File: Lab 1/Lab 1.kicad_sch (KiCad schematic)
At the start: 50 parts, among them K1 Fujitsu_FTR-LYCA005x, K10 Fujitsu_FTR-LYCA005x, K11 Fujitsu_FTR-LYCA005x, K12 Fujitsu_FTR-LYCA005x, K13 Fujitsu_FTR-LYCA005x, K14 Fujitsu_FTR-LYCA005x, K15 Fujitsu_FTR-LYCA005x, K2 Fujitsu_FTR-LYCA005x, K3 Fujitsu_FTR-LYCA005x, K4 Fujitsu_FTR-LYCA005x, K5 Fujitsu_FTR-LYCA005x, K6 Fujitsu_FTR-LYCA005x, K7 Fujitsu_FTR-LYCA005x, K8 Fujitsu_FTR-LYCA005x, K9 Fujitsu_FTR-LYCA005x, M1 Motor_DC, M2 Motor_DC, M3 Motor_DC, SW1 SW_Push, SW10 SW_Nidec_CAS-120A1, SW11 SW_Nidec_CAS-120A1, SW12 SW_Nidec_CAS-120A1, SW13 SW_Push, SW2 SW_Push_Open, SW3 SW_Push, SW4 SW_Push_Open, SW5 SW_Push, SW6 SW_Push, SW7 SW_Push, SW8 SW_Push, SW9 SW_Nidec_CAS-120A1

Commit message: Add fuses to A2-4
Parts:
- added F1, F2, F3: Fuse, symbol Device:Fuse
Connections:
- net at R4.2: now also F3.1; no longer D3.2 (A)
- net at R3.2: now also F2.1; no longer D2.2 (A)
- net at R2.2: now also F1.1; no longer D1.2 (A)
- new net: D2.2 (A), F2.2
- new net: D3.2 (A), F3.2
- new net: D1.2 (A), F1.2
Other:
- moved on the sheet: R2, R3

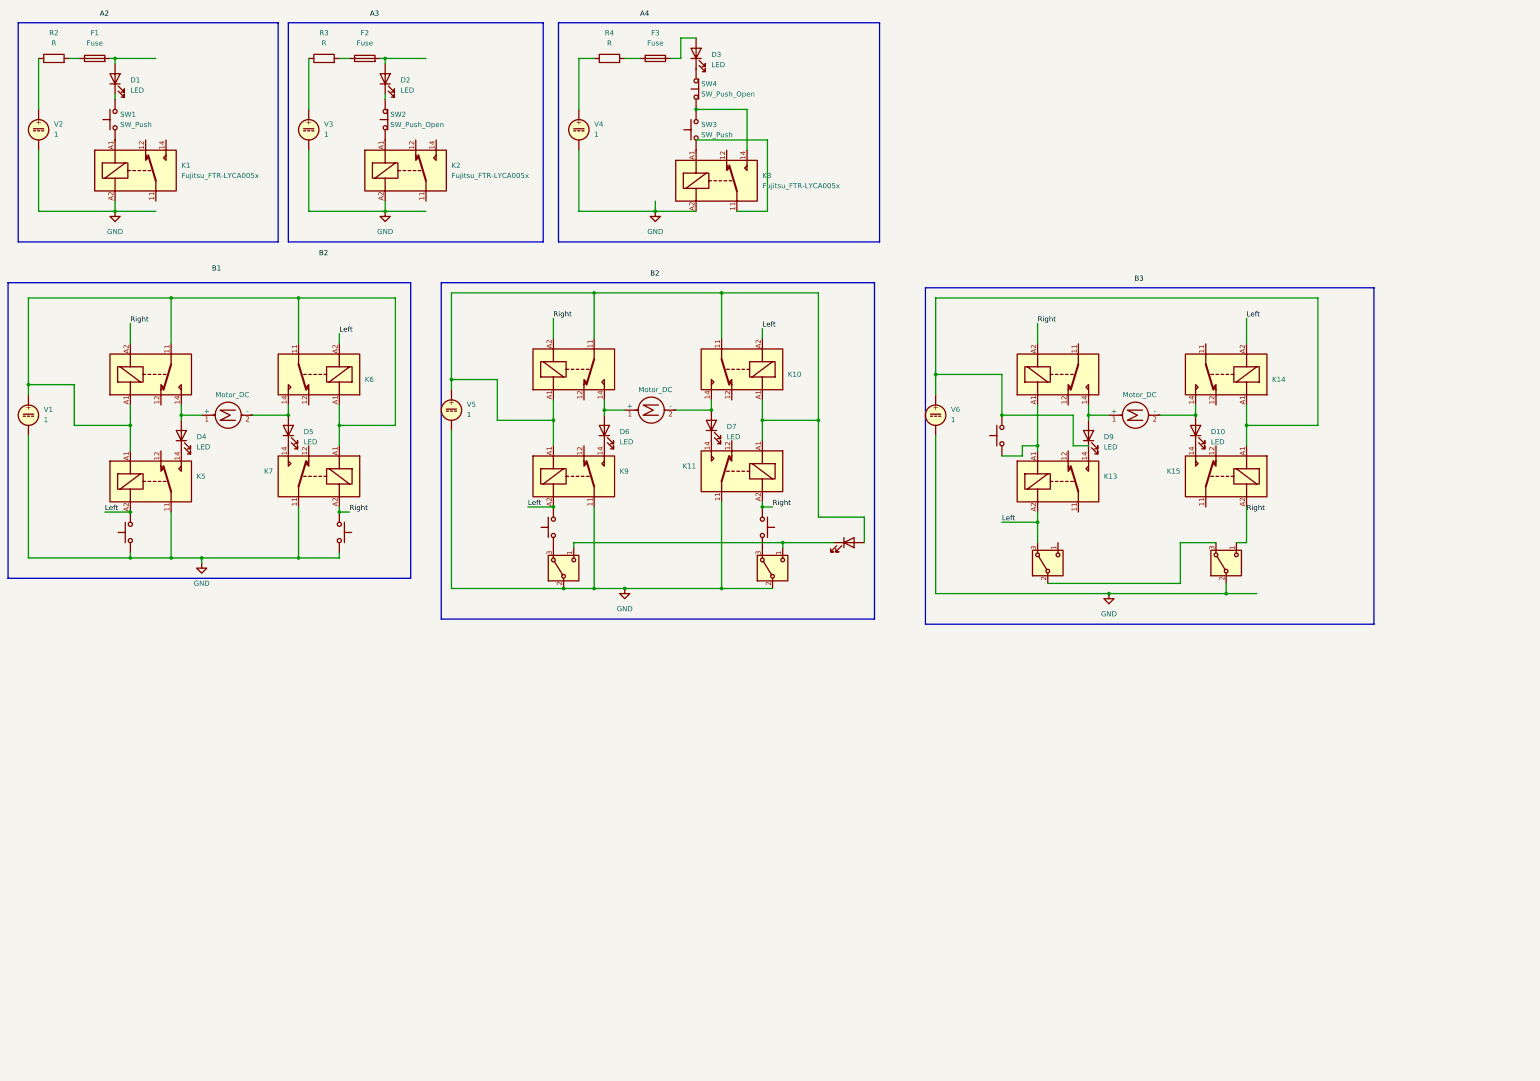
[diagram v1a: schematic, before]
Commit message: Redo B1 and B2 to use 2 relays
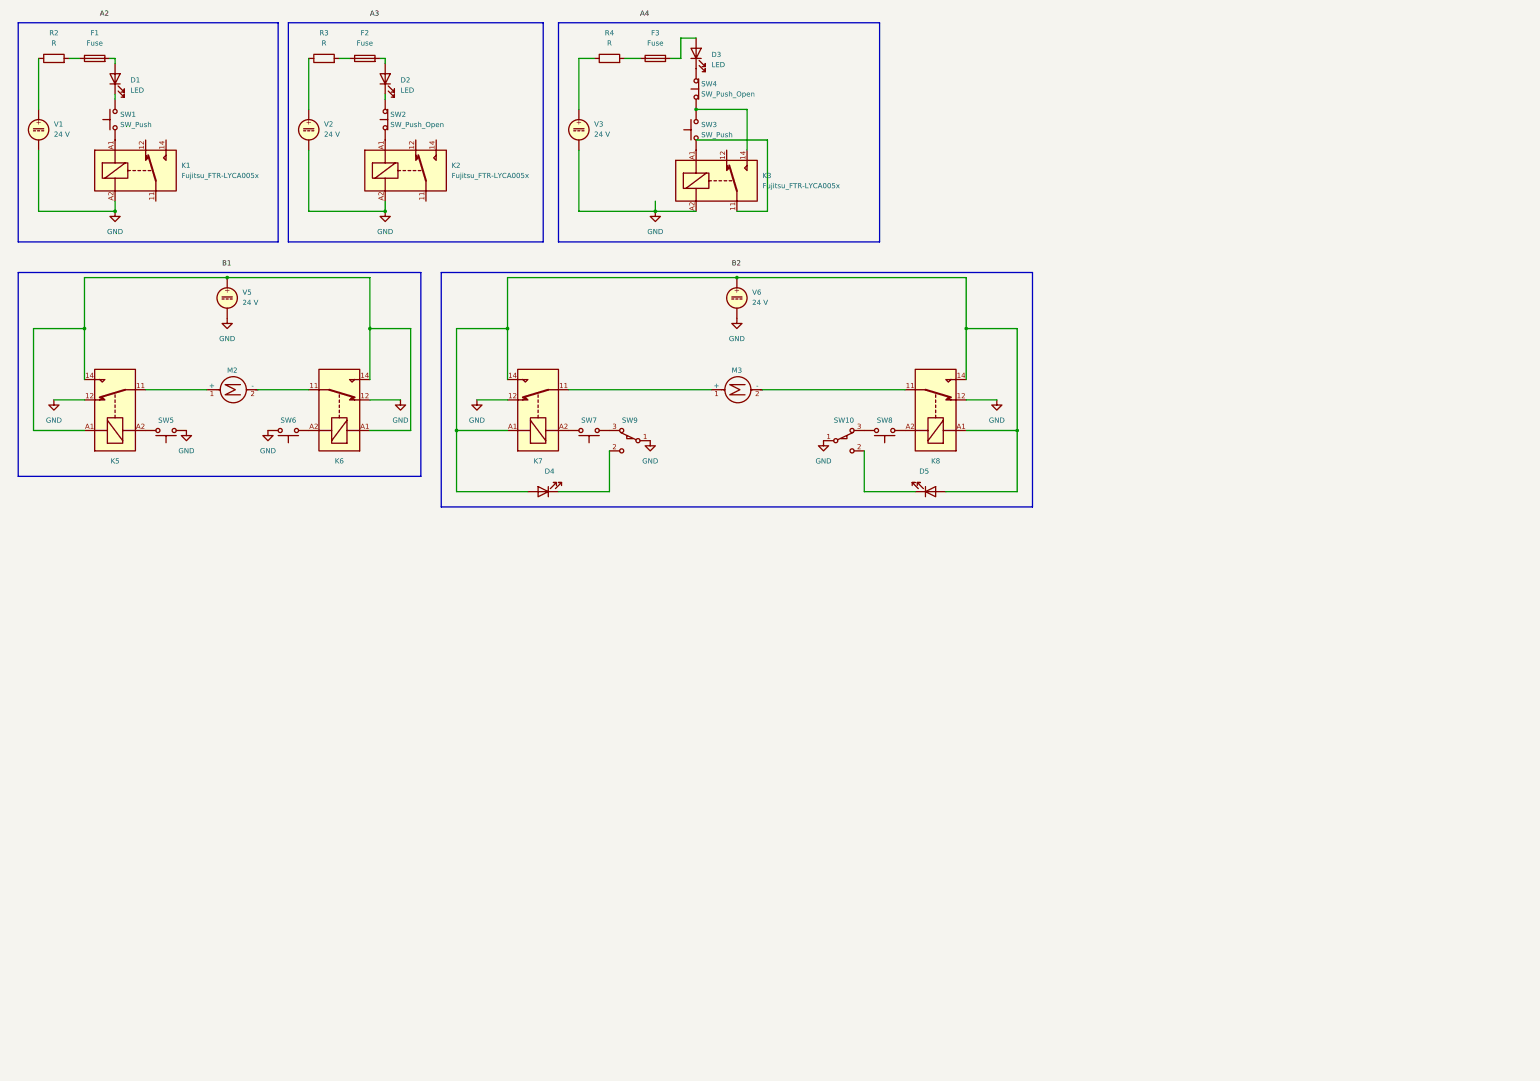
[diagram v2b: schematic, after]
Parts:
- removed D10, D6, D7, D8, D9: LED, symbol Device:LED
- removed K10, K11, K12, K13, K14, K15, K4, K9: Fujitsu_FTR-LYCA005x, Relay_THT:Relay_SPDT_Fujitsu_FTR-LYCA005x_FormC_Vertical, symbol Relay:Fujitsu_FTR-LYCA005x
- removed M1: Motor_DC, symbol Motor:Motor_DC
- removed SW10, SW11, SW12, SW9: SW_Nidec_CAS-120A1, Button_Switch_SMD:Nidec_Copal_CAS-120A, symbol Switch:SW_Nidec_CAS-120A1
- removed SW13: SW_Push, symbol Switch:SW_Push
- removed V1, V4: 1, symbol Simulation_SPICE:VDC
- added SW10, SW9: SW_SPDT_XKB_DMx-xxxx-1, symbol Switch:SW_SPDT_XKB_DMx-xxxx-1
- added V3: 24 V, symbol Simulation_SPICE:VDC
- V1: renamed from V2; value 1 -> 24 V
- V2: renamed from V3; value 1 -> 24 V
- V5, V6: value 1 -> 24 V
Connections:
- net GND: now also K5.12, K6.12, K7.12, K8.12, SW10.1 (A), SW9.1 (A), V3.2; no longer K5.11, K7.11
- net at R4.1: now also V3.1
- net at SW7.1: now also SW9.3 (C)
- net at K5.14: now also K5.A1, K6.14, K6.A1, V5.1; no longer D4.1 (K)
- net at D4.2 (A): now also D5.2 (A), K7.14, K7.A1, K8.14, K8.A1, V6.1
- net at M3.1 (+): now also K7.11
- net at M3.2 (-): now also K8.11
- net at M2.1 (+): now also K5.11; no longer K8.14
- net at SW8.1: now also SW10.3 (C)
- net at M2.2 (-): now also K6.11
- net at D5.1 (K): now also SW10.2 (B); no longer K7.14
- net Left: no longer names the net of K5.A2, SW5.2
- net Left: no longer K6.A2, SW7.2
- net Right: no longer names the net of K8.A2, SW8.2
- net Right: no longer K7.A2, SW6.2
- new net: K7.A2, SW7.2
- new net: K6.A2, SW6.2
- new net: D4.1 (K), SW9.2 (B)

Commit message: Add missing leds
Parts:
- added D4, D5, D6, D7: LED, symbol Device:LED
- renumbered D4 to D8, D5 to D9
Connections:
- net GND: now also D4.1 (K), D5.1 (K), D6.1 (K), D7.1 (K); no longer K5.12, K6.12, K7.12, K8.12
- new net: D5.2 (A), K5.12
- new net: D7.2 (A), K8.12
- new net: D6.2 (A), K7.12
- new net: D4.2 (A), K6.12

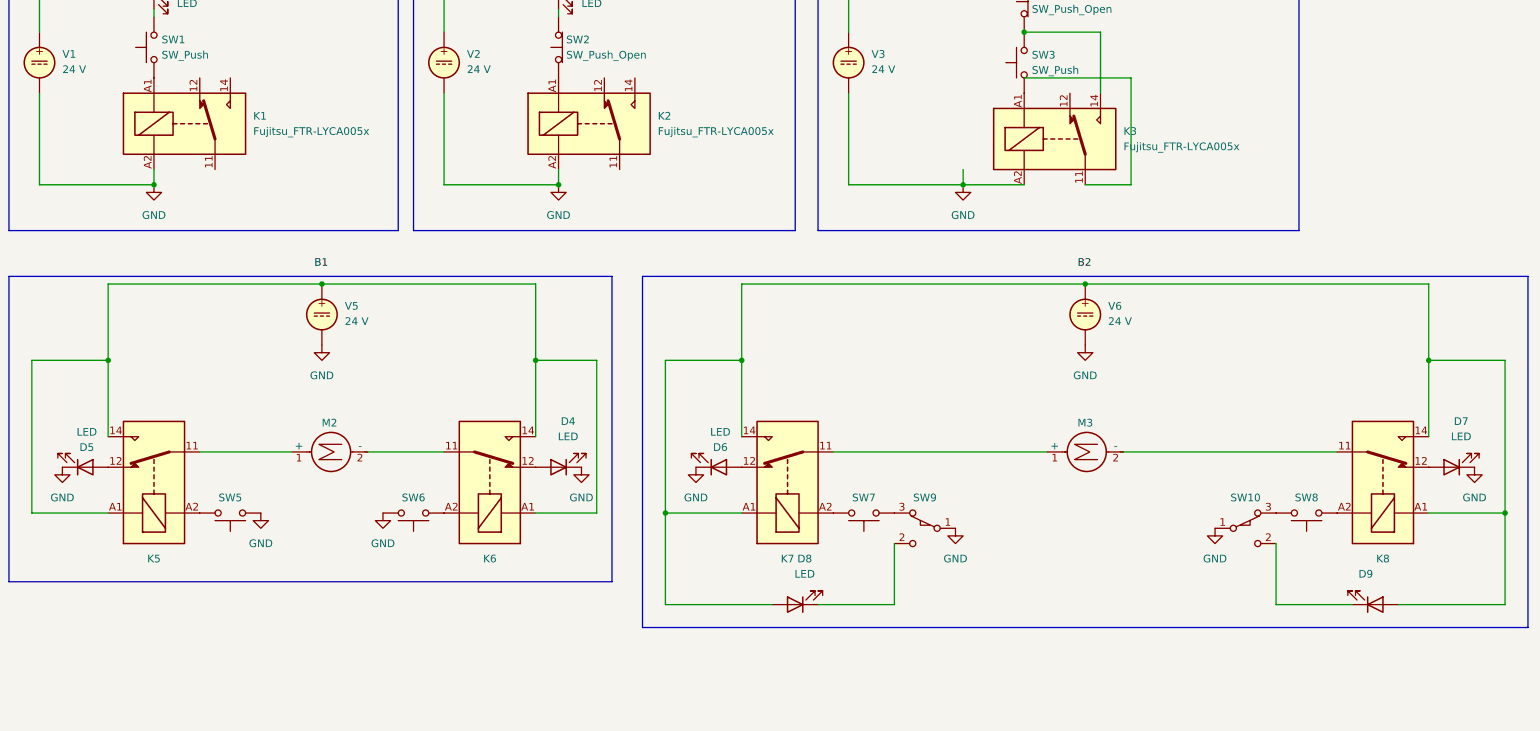
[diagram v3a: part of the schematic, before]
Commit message: Add START and STOP buttons to B2
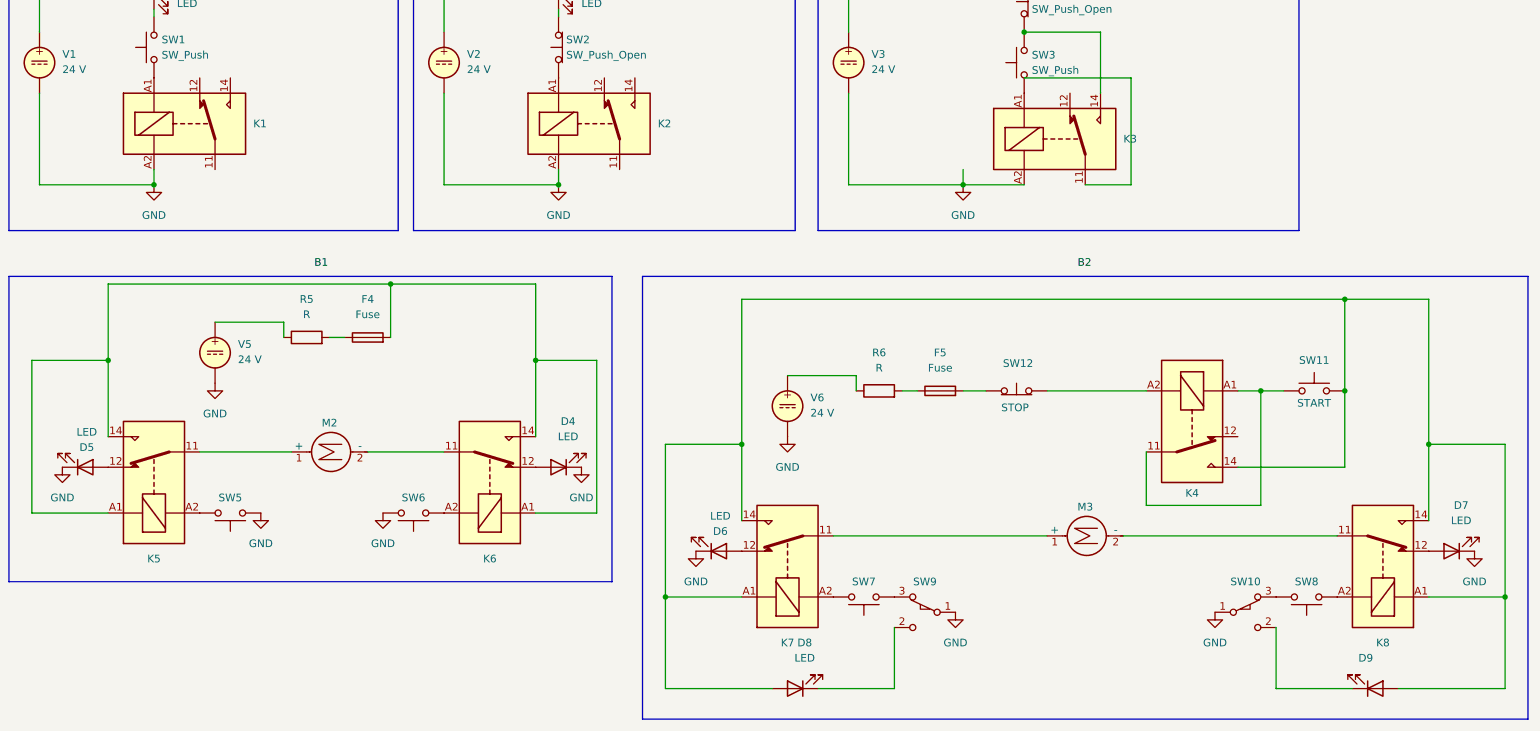
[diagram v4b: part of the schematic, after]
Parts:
- added F4, F5: Fuse, symbol Device:Fuse
- added K4: Fujitsu_FTR-LYCA005x, Relay_THT:Relay_SPDT_Fujitsu_FTR-LYCA005x_FormC_Vertical, symbol Relay:Fujitsu_FTR-LYCA005x
- added R5, R6: R, symbol Device:R
- added SW11: START, symbol Switch:SW_Push
- added SW12: STOP, symbol Switch:SW_Push_Open
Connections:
- net at K5.14, K5.A1, K6.14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: now also F4.2; no longer V5.1
- net at D8.2 (A), D9.2 (A), K7.14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: now also K4.14, SW11.2; no longer V6.1
- new net: K4.11, K4.A1, SW11.1
- new net: K4.A2, SW12.2 (B)
- new net: F4.1, R5.2
- new net: R5.1, V5.1
- new net: F5.2, SW12.1 (A)
- new net: R6.1, V6.1
- new net: F5.1, R6.2
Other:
- moved on the sheet: D6, D7, D8, D9, K7, K8, M3, SW10, SW7, SW8, SW9, V5

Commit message: Add B3
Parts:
- added D10, D11, D12, D13: LED, symbol Device:LED
- added F6: Fuse, symbol Device:Fuse
- added K10, K11, K12, K9: Fujitsu_FTR-LYCA005x, Relay_THT:Relay_SPDT_Fujitsu_FTR-LYCA005x_FormC_Vertical, symbol Relay:Fujitsu_FTR-LYCA005x
- added M4: Motor_DC, symbol Motor:Motor_DC
- added R7: R, symbol Device:R
- added SW13, SW14: SW_SPDT_XKB_DMx-xxxx-1, symbol Switch:SW_SPDT_XKB_DMx-xxxx-1
- added SW15: STOP, symbol Switch:SW_Push_Open
- added SW18: START, symbol Switch:SW_Push
- added V7: 24 V, symbol Simulation_SPICE:VDC
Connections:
- net GND: now also D10.1 (K), D11.1 (K), D12.1 (K), D13.1 (K), K12.11, V7.2
- new net: K11.A2, K12.14, K12.A1, SW14.1 (A)
- new net: D12.2 (A), SW14.2 (B)
- new net: K10.14, K11.14, K11.A1, K9.14, K9.A1, SW13.1 (A), SW18.2
- new net: D11.2 (A), SW13.2 (B)
- new net: K12.A2, SW13.3 (C)
- new net: R7.1, V7.1
- new net: F6.1, R7.2
- new net: K10.11, K10.A1, SW18.1
- new net: K10.A2, SW15.2 (B)
- new net: K12.12, K9.A2
- new net: K9.11, M4.1 (+)
- new net: D10.2 (A), K9.12
- new net: F6.2, SW15.1 (A)
- new net: K11.11, M4.2 (-)
- new net: D13.2 (A), K11.12

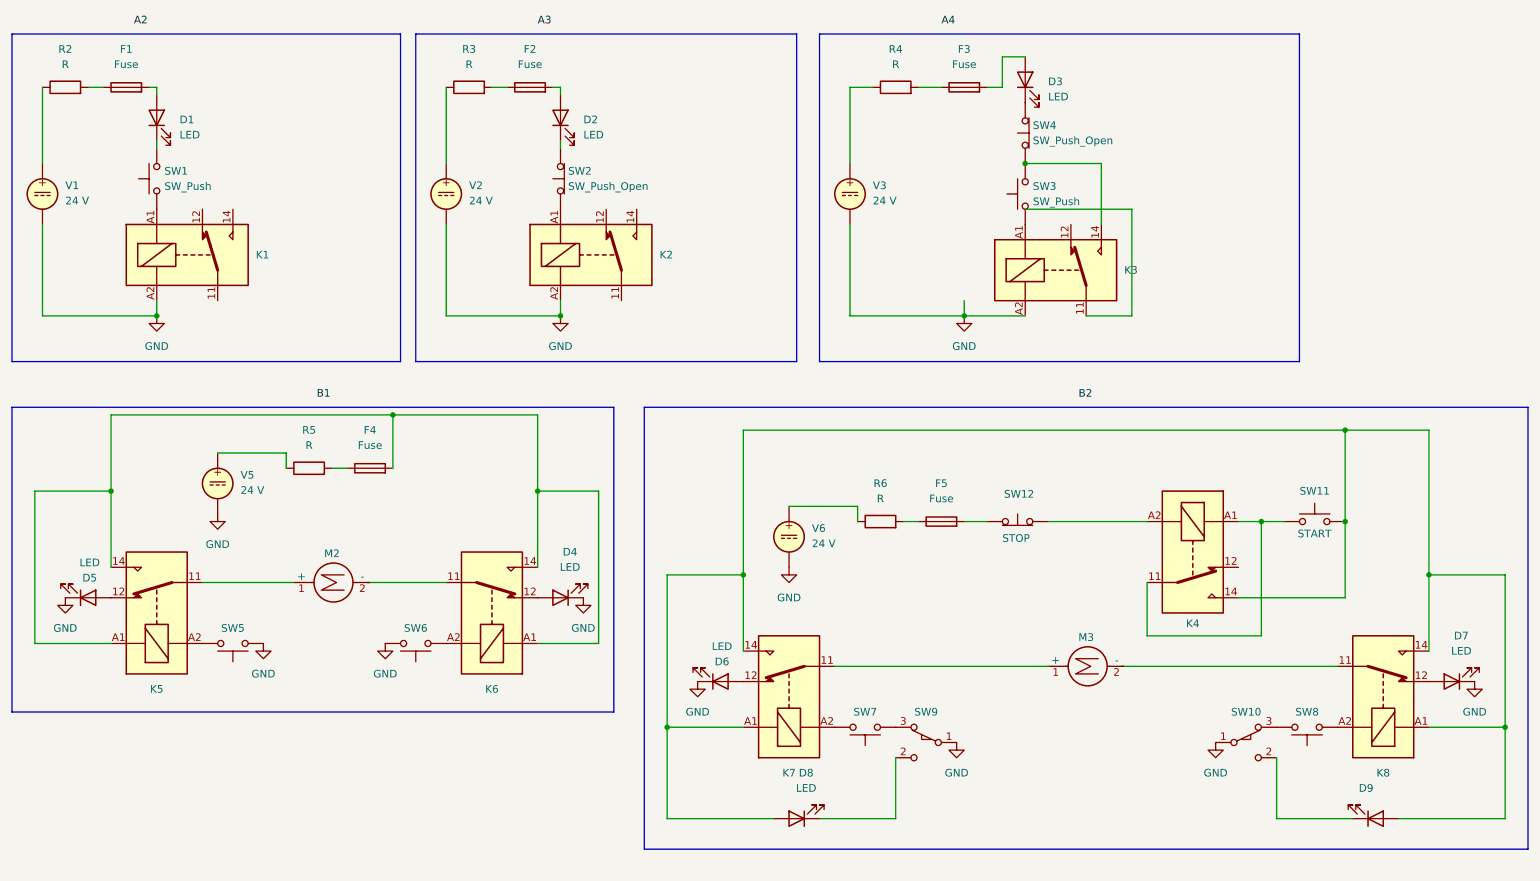
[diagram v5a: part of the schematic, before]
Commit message: Fix A2-4 and B1-2
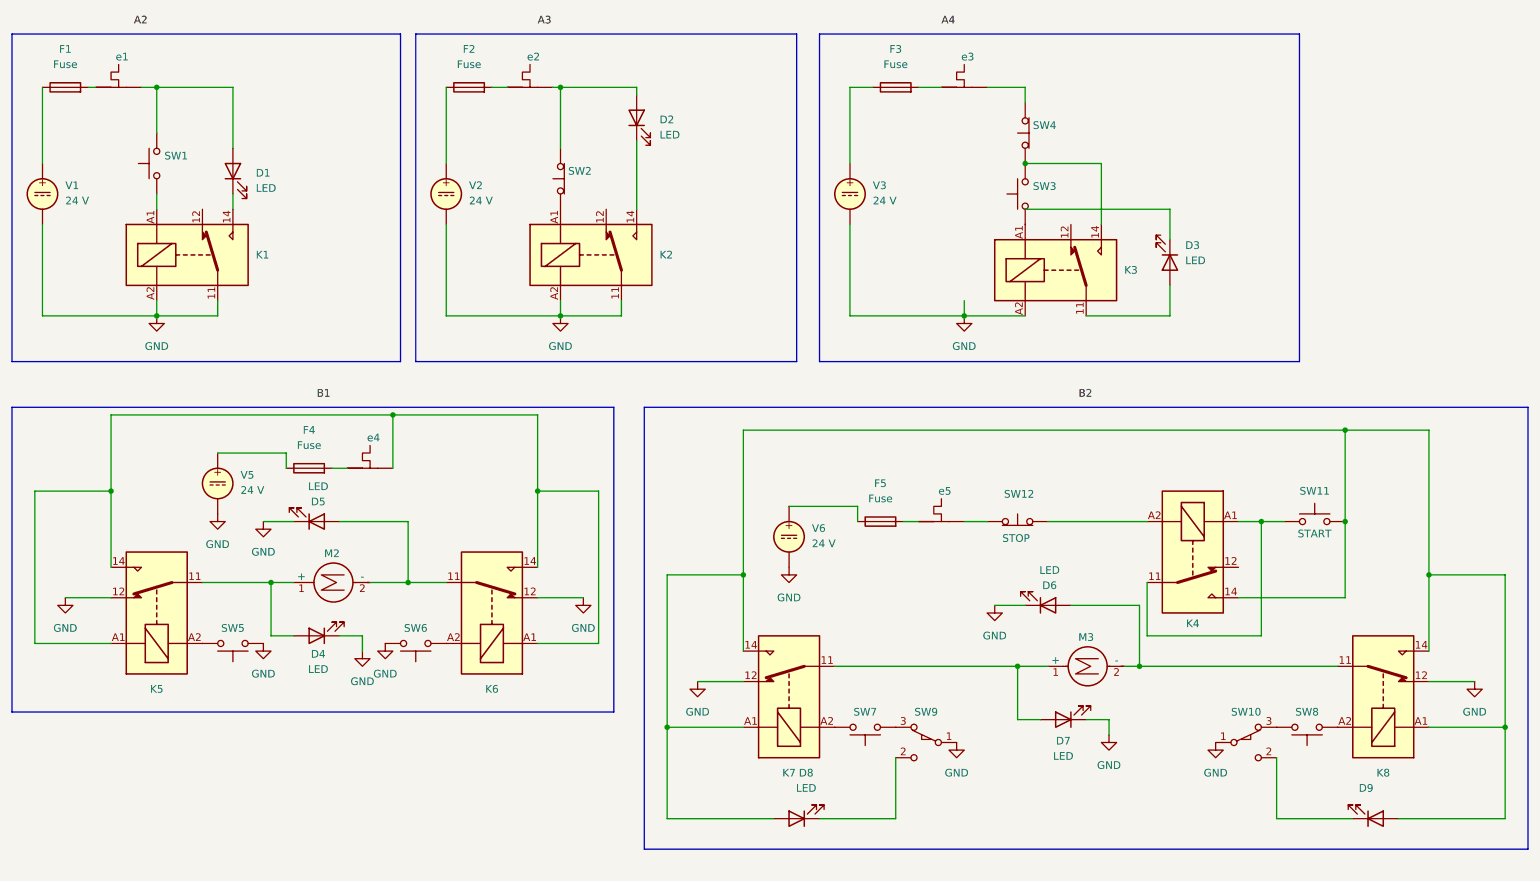
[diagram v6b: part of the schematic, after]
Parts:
- removed R2, R3, R4, R5, R6: R, symbol Device:R
- added e1, e2, e3, e4, e5: ~, symbol relay_contact:Thermal_Contact_NC
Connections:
- net GND: now also K1.11, K2.11, K5.12, K6.12, K7.12, K8.12
- net at K5.11, M2.1 (+): now also D4.2 (A)
- net at D5.2 (A): now also K6.11, M2.2 (-); no longer K5.12
- net at K5.14, K5.A1, K6.14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: no longer F4.2
- net at K3.11: now also D3.2 (A)
- net at V3.1: now also F3.1
- net at V2.1: now also F2.1
- net at K2.14: now also D2.1 (K)
- net at K8.11, M3.2 (-): now also D6.2 (A)
- net at D7.2 (A): now also K7.11, M3.1 (+); no longer K8.12
- net at F2.2: no longer D2.2 (A)
- net at SW2.2 (B): now also D2.2 (A); no longer D2.1 (K)
- net at F3.2: no longer D3.2 (A)
- net at F4.1: now also V5.1
- net at V1.1: now also F1.1
- net at D1.1 (K): now also K1.14; no longer SW1.2
- net at D1.2 (A): now also SW1.2; no longer F1.2
- net at SW4.2 (B): no longer D3.1 (K)
- net at SW12.1 (A): no longer F5.2
- net at V6.1: now also F5.1
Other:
- moved on the sheet: D1, D2, D3, D4, D5, D6, D7, F1, F2, F3, F4, F5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
